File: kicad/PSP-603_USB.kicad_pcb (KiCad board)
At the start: 2 copper layers, 35.5 x 33 mm, 39 parts, among them J1 10118193-0001LF, J2 826947-4, J3 5019, M1 9575, M2 9575, U1 93LC56BT-I/OT, U2 FT232HL-Reel, U3 SN74LV1T34DBVR, X1 ABM8G-12.000MHZ-18-D2Y-T

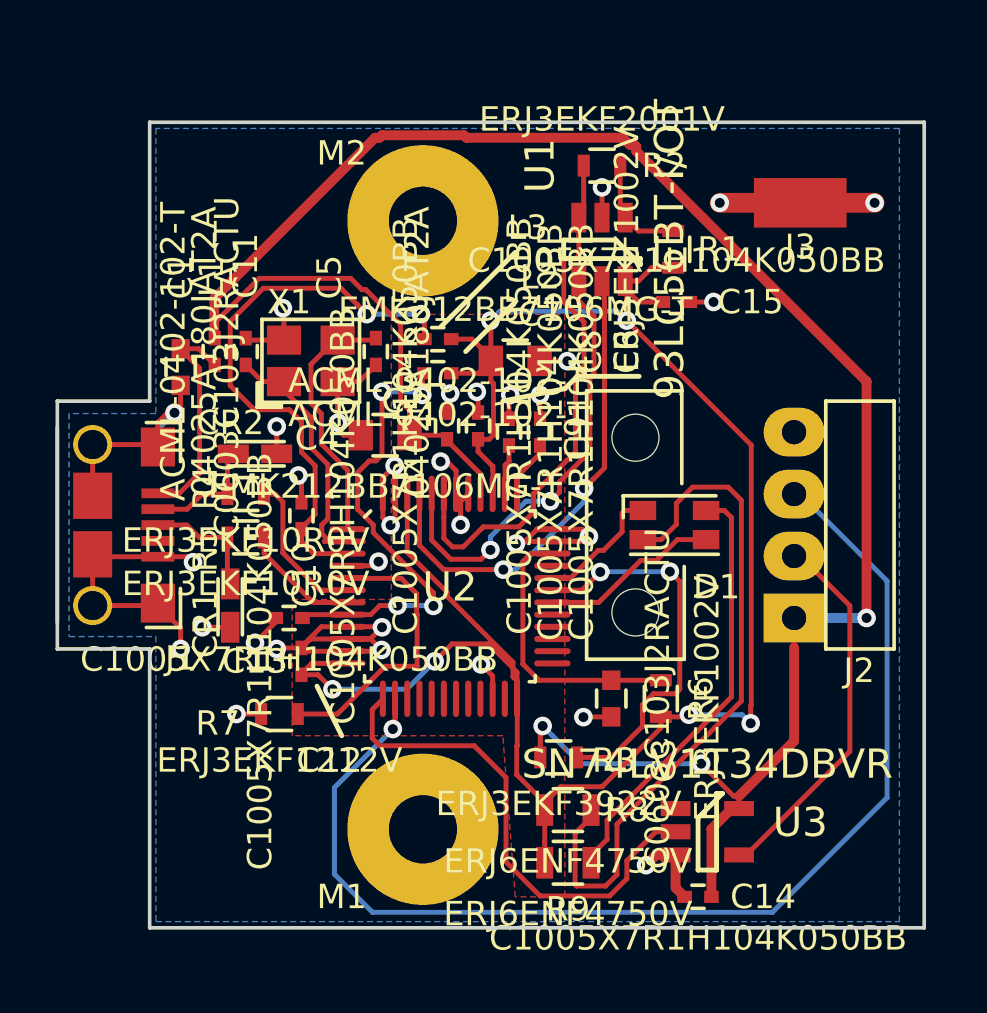
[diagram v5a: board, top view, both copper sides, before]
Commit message: Switched to FT232R
Signed-off-by: Chris Stook <chris@chrisstook.com>
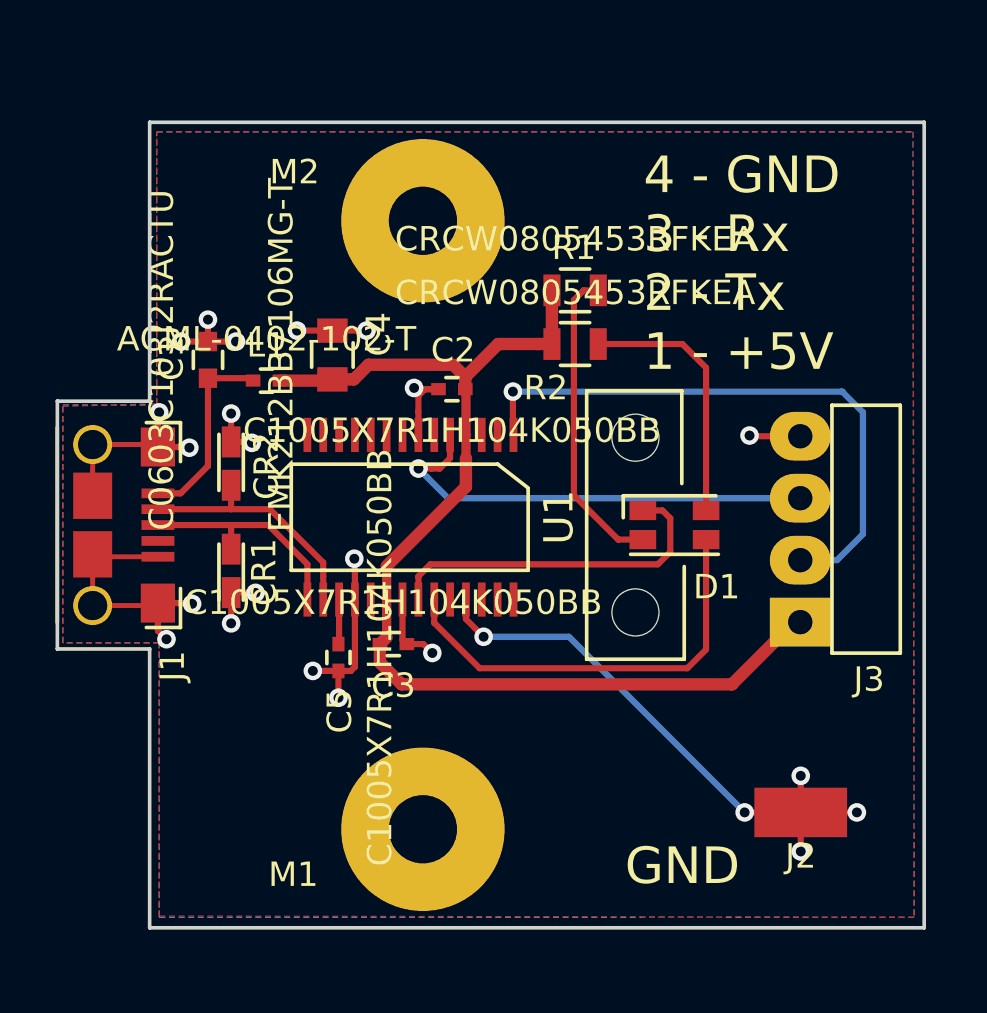
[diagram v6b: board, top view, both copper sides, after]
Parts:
- removed C10, C12, C13, C14, C15, C6, C8, C9: C1005X7R1H104K050BB, Standard_Footprints:C0402
- removed C11: 04025A180JAT2A, Standard_Footprints:C0402
- removed C7: EMK212BB7106MG-T, Standard_Footprints:C0805
- removed L2, L3: ACML-0402-102-T, Standard_Footprints:C0402
- removed R3: ERJ3EKF3922V, Standard_Footprints:R0603
- removed R4, R5: ERJ3EKF10R0V, Standard_Footprints:R0603
- removed R6: ERJ3EKF1002V, Standard_Footprints:R0603
- removed R7: ERJ3EKF1212V, Standard_Footprints:R0603
- removed R8, R9: ERJ6ENF4750V, Standard_Footprints:R0805
- removed U2: FT232HL-Reel, FTDI_Footprints:LQFP_48
- removed U3: SN74LV1T34DBVR, Standard_Footprints:TSOT-23-5
- removed X1: ABM8G-12.000MHZ-18-D2Y-T, Abracon_Footprints:ABM8G
- C3: value C0603C103J2RACTU -> C1005X7R1H104K050BB; footprint Standard_Footprints:C0603 -> Standard_Footprints:C0402
- C5: value 04025A180JAT2A -> C1005X7R1H104K050BB
- J2: value 826947-4 -> 5019; footprint TE_Connectivity_Footprints:826947-4 -> Keystone_Electronics_Footprints:5090
- J3: value 5019 -> 826947-4; footprint Keystone_Electronics_Footprints:5090 -> TE_Connectivity_Footprints:826947-4
- R1: value ERJ3EKF1002V -> CRCW0805453RFKEA; footprint Standard_Footprints:R0603 -> Standard_Footprints:R0805
- R2: value ERJ3EKF2001V -> CRCW0805453RFKEA; footprint Standard_Footprints:R0603 -> Standard_Footprints:R0805
- U1: value 93LC56BT-I/OT -> FT232RL-REEL; footprint Standard_Footprints:TSOT-32-6 -> FTDI_Footprints:SSOP-28
- moved U1 13.5 mm to (141.5, 108.9), turned to 180 degrees
- moved J3 13.4 mm to (157.5, 109.4), turned to 90 degrees
- moved C5 12.6 mm to (138.6, 114.7)
- moved J2 11.8 mm to (157.5, 121.0), turned to 0 degrees
- moved C3 9.21 mm to (140.8, 114.1), turned to 180 degrees
- moved R2 7.39 mm to (148.2, 101.8)
- moved R1 4.36 mm to (148.2, 99.6), turned to 180 degrees
- moved C4 3.93 mm to (138.3, 102.2), turned to 270 degrees
- moved L1 2.43 mm to (135.6, 103.3), turned to 180 degrees
- moved C2 1.52 mm to (143.2, 103.7), turned to 0 degrees
- moved CR1 1.42 mm to (134.2, 111.1)
- moved C1 1.16 mm to (133.2, 102.5), turned to 270 degrees
- moved CR2 1.06 mm to (134.2, 106.7), turned to 90 degrees
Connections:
- C3 pad 2: Net-(C3-Pad2) -> /VBUS
- D1 pad 1: Net-(D1-Pad1) -> /RXLED
- D1 pad 3: Net-(D1-Pad3) -> /TXLED
- J2 pad 1: /VBUS -> GND
- J3 pad 1: GND -> /VBUS
- R1 pad 1: /EE_DO -> Net-(D1-Pad4)
- R1 pad 2: /VCCD -> /VBUS
- R2 pad 1: /EE_DO -> Net-(D1-Pad2)
- R2 pad 2: /EE_DATA -> /VBUS
- U1 pad 1: /EE_DO -> /UART_TX
- U1 pad 2: GND -> Net-(U1-Pad2)
- U1 pad 3: /EE_DATA -> Net-(U1-Pad3)
- U1 pad 4: /EE_CLK -> /VBUS
- U1 pad 5: /EE_CS -> /UART_RX
- U1 pad 6: /VCCD -> Net-(U1-Pad6)
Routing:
- net /VCCD: track 83.0 -> 0.00 mm, vias 6 -> 0
- net /VBUS: track 90.5 -> 46.2 mm, vias 3 -> 0
- net /UART_RX: track 47.6 -> 18.6 mm
- net /VPHY: track 23.5 -> 0.00 mm, vias 2 -> 0
- net /EE_DATA: track 22.2 -> 0.00 mm
- net Net-(U2-Pad13): track 20.5 -> 0.00 mm
- net /EE_CS: track 19.9 -> 0.00 mm, vias 2 -> 0
- net /VPLL: track 18.8 -> 0.00 mm, vias 4 -> 0
- net /EE_CLK: track 18.4 -> 0.00 mm, vias 2 -> 0
- net /TXLED: track 0.00 -> 17.7 mm
- net GND: track 86.1 -> 69.9 mm, vias 32 -> 24
- net /VBUSDTCT: track 16.0 -> 0.00 mm, vias 2 -> 0
- net Net-(D1-Pad4): track 28.4 -> 12.7 mm
- net /RXLED: track 0.00 -> 14.3 mm
- net Net-(R7-Pad2): track 11.8 -> 0.00 mm
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- added copper zone on F.Cu, net GND
- removed copper zone on F.Cu, net /VCCD
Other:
- net class Default: clearance 0.2032 -> 0.1524; trace_width 0.2032 -> 0.254
- net class power added: clearance 0.254, trace_width 0.508, via_dia 0.762, via_drill 0.4064
- rule trace_clearance: 0.2032 -> 0.1524
- board text added: "4 - GND 3 - Rx 2 - Tx 1 - +5V"
- board text added: "GND"
- board text added: "PSP-603 USB 3/25/2016"

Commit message: redo layout Signed-off-by: Chris Stook <chris@chrisstook.com>
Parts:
- moved R2 5.02 mm to (150.2, 97.2)
- moved C1 3.66 mm to (136.8, 102.7)
- moved L1 3.31 mm to (138.9, 103.6)
- moved C4 3.06 mm to (141.3, 102.5)
- moved CR1 2.05 mm to (136.2, 111.0)
- moved CR2 2.05 mm to (136.2, 106.8)
- moved R1 2.02 mm to (150.2, 99.8)
- moved J1 1.50 mm to (130.0, 109.2)
- moved C3 1.26 mm to (142.1, 114.0)
- moved U1 1.20 mm to (142.7, 108.8)
- moved C5 1.06 mm to (139.6, 114.3)
- moved C2 0.84 mm to (144.0, 103.9)
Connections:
- net Net-(C1-Pad2) renamed /+5v
- net Net-(C5-Pad2) renamed /3r3v
- net Net-(CR1-Pad1) renamed /D+
- net Net-(CR2-Pad1) renamed /D-
- net Net-(D1-Pad2) renamed /RXLEDANNODE
- net Net-(D1-Pad4) renamed /TXLEDANNODE
- J1 pad 10: GND -> /Shield
- J1 pad 11: GND -> /Shield
- J1 pad 6: GND -> /Shield
- J1 pad 7: GND -> /Shield
- J1 pad 8: GND -> /Shield
- J1 pad 9: GND -> /Shield
- M1 pad 1: Net-(M1-Pad1) -> GND
- M2 pad 1: Net-(M2-Pad1) -> GND
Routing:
- net /Shield: track 0.00 -> 12.0 mm
- net GND: track 69.9 -> 58.3 mm, vias 24 -> 26
- net /TXLED: track 17.7 -> 11.9 mm
- net /RXLED: track 14.3 -> 10.1 mm
- net /UART_RX: track 18.6 -> 15.8 mm
- net /RXLEDANNODE: track 10.7 -> 12.8 mm
- net /UART_TX: track 24.7 -> 23.0 mm
- net /TXLEDANNODE: track 12.7 -> 11.7 mm
- net /+5v: track 8.01 -> 9.02 mm
- removed copper zone on F.Cu, net GND
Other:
- board size 35.5 x 33 mm -> 34 x 33 mm
- board text added: "4 GND 3 Rx 2 Tx 1 +5V"
- board text added: "PSP-603 USB 3/26/2016"
- board text removed: "4 - GND 3 - Rx 2 - Tx 1 - +5V"
- board text removed: "PSP-603 USB 3/25/2016"

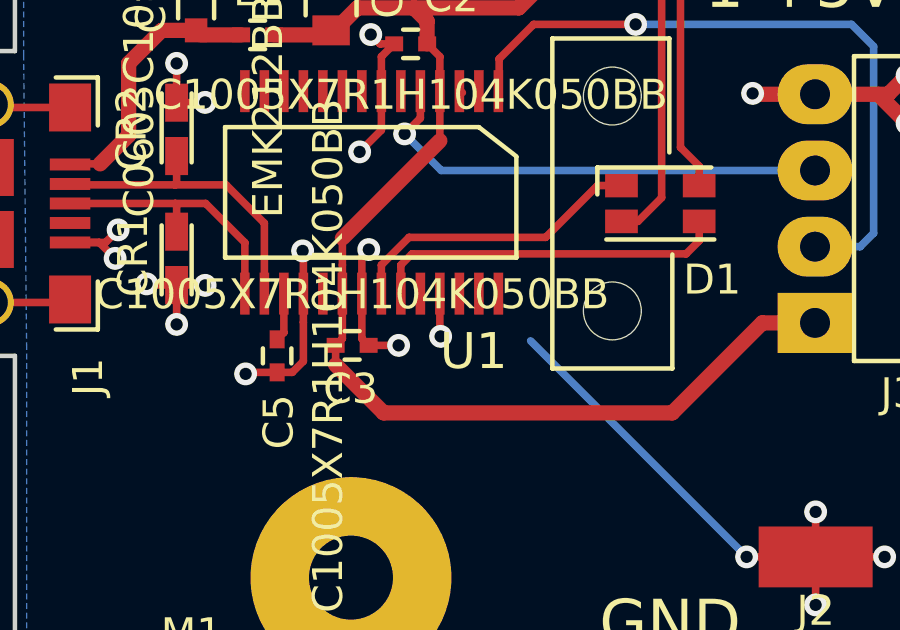
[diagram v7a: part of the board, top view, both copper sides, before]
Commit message: tied test pin to gnd.
Signed-off-by: Chris Stook <chris@chrisstook.com>
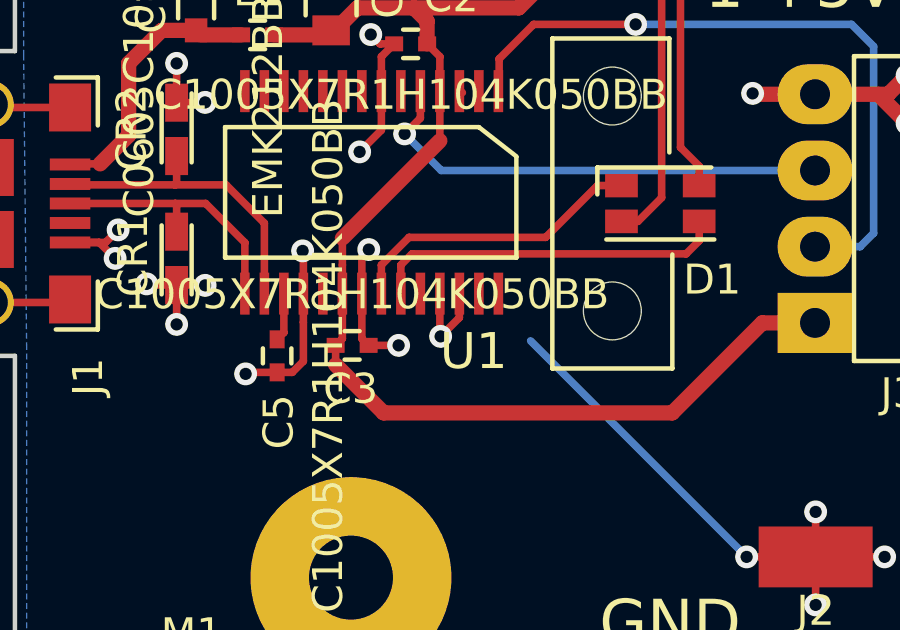
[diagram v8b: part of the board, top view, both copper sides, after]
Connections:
- U1 pad 26: Net-(U1-Pad26) -> GND
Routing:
- net GND: track 58.3 -> 60.0 mm
